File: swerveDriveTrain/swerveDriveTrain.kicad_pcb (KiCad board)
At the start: 4 copper layers, 55 x 125.6 mm, 39 parts, among them IC1 TCAN3414DR, J1 RJ45, J2 Screw_Terminal_01x02, J3 Conn_01x06_Pin, J4 S6B-PH-K-S_LF__SN_, U2 Teensy4.0

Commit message: new outline
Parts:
- J4: moved to B.Cu
- moved J2 215.5 mm to (227.8, 144.4), turned to 0 degrees
- moved U2 211.9 mm to (238.3, 85.1)
- moved J4 186.7 mm to (232.5, 30.7), turned to -90 degrees
- moved U3 185.3 mm to (223.2, 108.4), turned to -90 degrees
- moved J3 178.7 mm to (224.6, 135.0)
- moved U1 135.6 mm to (171.4, 108.3), turned to -90 degrees
- moved J1 135.3 mm to (193.1, 131.6)
- moved IC1 135.3 mm to (197.9, 137.6), turned to 90 degrees
- moved C4 52.2 mm to (113.1, 115.8)
- moved C1 30.2 mm to (115.3, 55.5)
- moved C2 30.2 mm to (115.3, 58.5)
- moved C3 30.2 mm to (115.3, 61.6)
- moved D1 30.2 mm to (139.1, 68.5)
- moved D2 30.2 mm to (139.1, 73.6)
- moved D3 30.2 mm to (139.1, 78.8)
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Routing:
- net +5V: track 109.8 -> 0.00 mm, vias 2 -> 0
- net CAN3v3: track 85.6 -> 0.00 mm, vias 1 -> 0
- net CTX: track 74.7 -> 0.00 mm
- net CRX: track 70.5 -> 0.00 mm
- net M2B: track 43.2 -> 0.00 mm
- net M2A: track 32.8 -> 0.00 mm
- net M1B: track 13.0 -> 0.00 mm
- net M1A: track 9.03 -> 0.00 mm
- net CANN: track 4.70 -> 8.14 mm
- net CANP: track 6.54 -> 7.80 mm
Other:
- board size 55 x 125.6 mm -> 82.5 x 125.6 mm

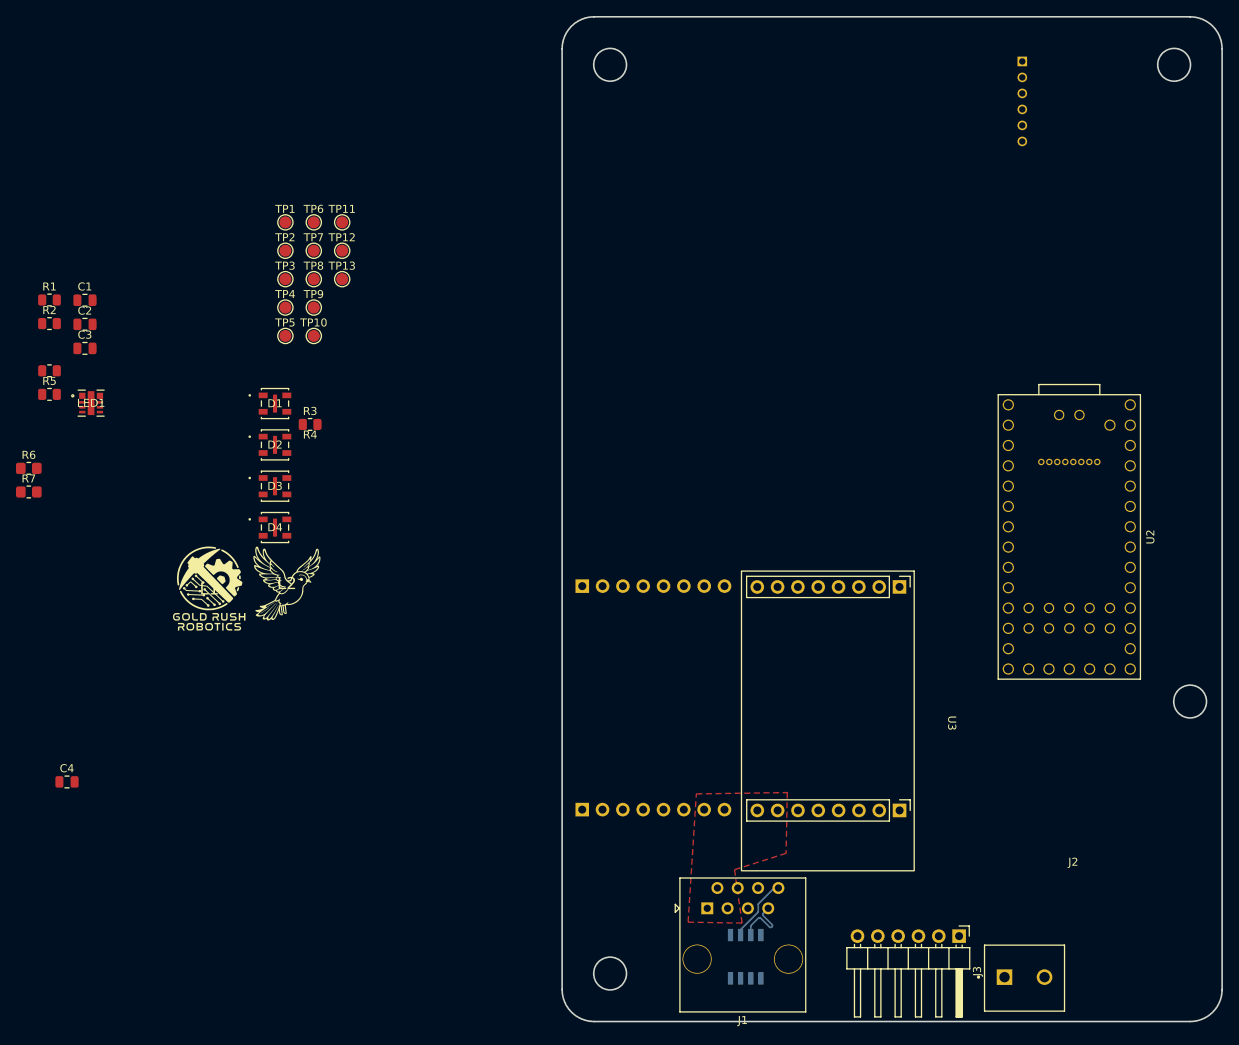
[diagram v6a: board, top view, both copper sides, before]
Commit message: finished first layout and routing pass
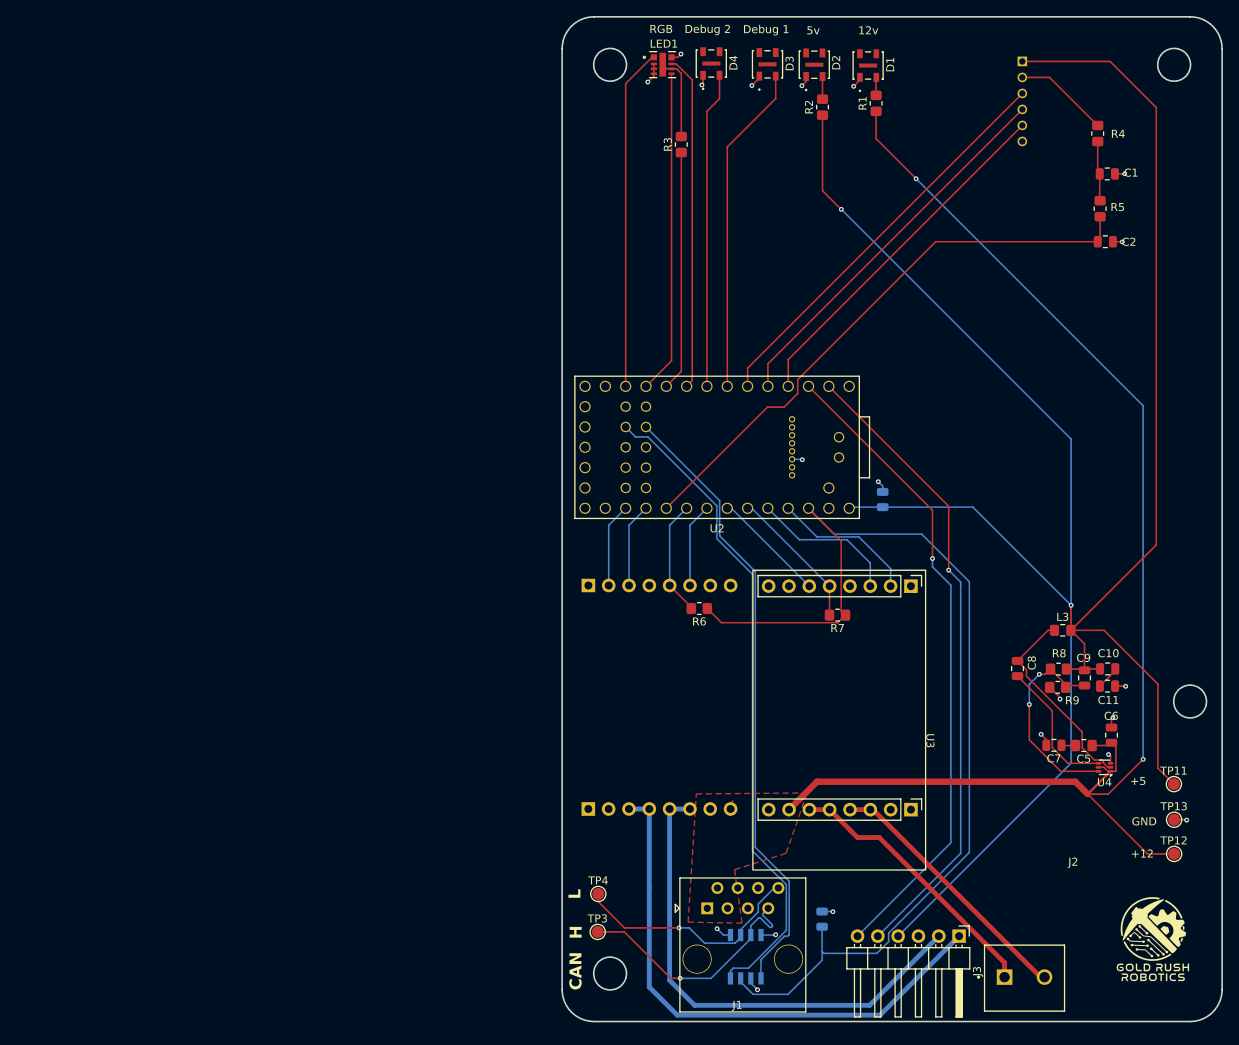
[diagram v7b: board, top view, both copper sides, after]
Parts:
- removed TP1, TP10, TP2, TP5, TP6, TP7, TP8, TP9: TestPoint_Probe, TestPoint:TestPoint_Pad_D1.5mm
- added C10: 22uF, Capacitor_SMD:C_0805_2012Metric, F.Cu at (243.2, 101.6)
- added C11: 22uF, Capacitor_SMD:C_0805_2012Metric, F.Cu at (243.1, 103.8)
- added C5: 10uF, Capacitor_SMD:C_0805_2012Metric_Pad1.18x1.45mm_HandSolder, F.Cu at (240.2, 111.2)
- added C6: 100nF, Capacitor_SMD:C_0805_2012Metric, F.Cu at (243.6, 109.9)
- added C7: 10uF, Capacitor_SMD:C_0805_2012Metric, F.Cu at (236.4, 111.2)
- added C8: 100nF, Capacitor_SMD:C_0805_2012Metric, F.Cu at (231.9, 101.6)
- added C9: 22pF, Capacitor_SMD:C_0805_2012Metric, F.Cu at (240.2, 102.8)
- added L3: 4.7uH, Inductor_SMD:L_0805_2012Metric_Pad1.15x1.40mm_HandSolder, F.Cu at (237.5, 96.8)
- added R8: 52.3kΩ, Resistor_SMD:R_0805_2012Metric_Pad1.20x1.40mm_HandSolder, F.Cu at (237.0, 101.7)
- added R9: 10kΩ, Resistor_SMD:R_0805_2012Metric_Pad1.20x1.40mm_HandSolder, F.Cu at (236.9, 103.9)
- added U4: TPS562202, Package_TO_SOT_SMD:SOT-563, F.Cu at (242.8, 113.9)
- C3, C4, L2: moved to B.Cu
- R1, R2, R3, R4, R5: footprint Resistor_SMD:R_0805_2012Metric -> Resistor_SMD:R_0805_2012Metric_Pad1.20x1.40mm_HandSolder
- moved R4 134.3 mm to (241.9, 34.7), turned to -90 degrees
- moved R5 133.4 mm to (242.2, 44.1), turned to -90 degrees
- moved C1 128.8 mm to (243.1, 39.8), turned to 180 degrees
- moved TP12 128.4 mm to (251.4, 124.8)
- moved C2 128.0 mm to (242.8, 48.2)
- moved L1 125.8 mm to (248.8, 135.4)
- moved TP11 125.5 mm to (251.4, 116.0)
- moved TP13 124.0 mm to (251.4, 120.5)
- moved R1 106.2 mm to (214.2, 30.9), turned to 90 degrees
- moved R7 102.3 mm to (209.4, 94.9), turned to 180 degrees
- moved C3 101.5 mm to (215.0, 80.5), turned to 90 degrees
- moved R2 100.3 mm to (207.5, 31.4), turned to 90 degrees
- moved C4 95.9 mm to (207.4, 132.9), turned to -90 degrees
- moved TP3 90.5 mm to (179.4, 134.5)
- moved L2 88.9 mm to (228.2, 76.2), turned to 180 degrees
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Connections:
- R6 pad 1: +3.3V -> CAN3v3
- R7 pad 1: +3.3V -> CAN3v3
- U2 pad 10: ENC1A -> RGBR
- U2 pad 11: ENC1B -> RGBG
- U2 pad 12: ENC2I -> RGBW
- U2 pad 13: ENC2A -> unconnected-(U2-11_MOSI_CTX1-Pad13)
- U2 pad 14: ENC2B -> unconnected-(U2-12_MISO_MQSL-Pad14)
- U2 pad 2: PWM1 -> ENC1A
- U2 pad 21: ABSA -> unconnected-(U2-14_A0_TX3_SPDIF_OUT-Pad21)
- U2 pad 22: CSM1 -> DIR1
- U2 pad 23: CSM2 -> PWM1
- U2 pad 24: unconnected-(U2-17_A3_TX4_SDA1-Pad24) -> ABSA
- U2 pad 25: DIR1 -> FLTM1
- U2 pad 26: DIR2 -> CSM1
- U2 pad 27: FLTM1 -> CSM2
- U2 pad 29: unconnected-(U2-22_A8_CTX1-Pad29) -> PWM2
- U2 pad 3: PWM2 -> ENC1B
- U2 pad 30: unconnected-(U2-23_A9_CRX1_MCLK1-Pad30) -> DIR2
- U2 pad 4: RGBR -> ENC2I
- U2 pad 5: RGBG -> ENC2B
- U2 pad 6: RGBB -> ENC2A
- U2 pad 7: RGBW -> LED1
- U2 pad 8: LED1 -> LED2
- U2 pad 9: LED2 -> RGBB
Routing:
- net +5V: track 0.00 -> 286.4 mm, vias 0 -> 2
- net +12V: track 0.00 -> 171.1 mm, vias 0 -> 2
- net CAN3v3: track 0.00 -> 133.0 mm
- net CRX: track 0.00 -> 82.2 mm
- net ENC1B: track 0.00 -> 80.9 mm, vias 0 -> 1
- net ENC1A: track 0.00 -> 79.8 mm, vias 0 -> 1
- net CTX: track 0.00 -> 78.0 mm
- net ABSA: track 0.00 -> 72.0 mm
- net M1A: track 0.00 -> 69.1 mm
- net M1B: track 0.00 -> 62.5 mm
- net ENC2A: track 0.00 -> 50.8 mm
- net ENC2B: track 0.00 -> 47.8 mm
- net ENC2I: track 0.00 -> 44.7 mm
- net RGBW: track 0.00 -> 42.7 mm
- net RGBB: track 0.00 -> 42.0 mm
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- added copper zone on In1.Cu, net GND
- added copper zone on In2.Cu, net GND
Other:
- board text added: "+12"
- board text added: "+5"
- board text added: "12v"
- board text added: "5v"
- board text added: "CAN"
- board text added: "Debug 1"
- board text added: "Debug 2"
- board text added: "GND"
- board text added: "H"
- board text added: "L"
- board text added: "RGB"

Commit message: cleaning
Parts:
- removed C10, C11: 22uF, Capacitor_SMD:C_0805_2012Metric
- removed C5: 10uF, Capacitor_SMD:C_0805_2012Metric_Pad1.18x1.45mm_HandSolder
- removed C6, C8: 100nF, Capacitor_SMD:C_0805_2012Metric
- removed C7: 10uF, Capacitor_SMD:C_0805_2012Metric
- removed C9: 22pF, Capacitor_SMD:C_0805_2012Metric
- removed L3: 4.7uH, Inductor_SMD:L_0805_2012Metric_Pad1.15x1.40mm_HandSolder
- removed LED1: 599-2310-427F, footprints:599-2310_DIA
- removed R9: 10kΩ, Resistor_SMD:R_0805_2012Metric_Pad1.20x1.40mm_HandSolder
- removed TP3, TP4: TestPoint_Probe, TestPoint:TestPoint_Pad_D1.5mm
- removed U4: TPS562202, Package_TO_SOT_SMD:SOT-563
- C1, C2, C3, C4: footprint Capacitor_SMD:C_0805_2012Metric -> Capacitor_SMD:C_0805_2012Metric_Pad1.18x1.45mm_HandSolder
- D1, D2, D3, D4: footprint GreenLED:LED_CREE_MLXXXX -> LED_SMD:LED_0805_2012Metric_Pad1.15x1.40mm_HandSolder
- R1: value 25 -> 500
- R2: value 5 -> 150
- R3: value 15 -> 50
- R6, R7: value R -> 10k
- R8: value 52.3kΩ -> 50
- U1, U3: value ~ -> G218v17
- moved R8 81.0 mm to (195.2, 32.3), turned to -90 degrees
- moved C4 13.3 mm to (198.1, 142.3), turned to 180 degrees
- moved R3 9.17 mm to (198.2, 32.3), turned to -90 degrees
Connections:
- D3 pad 2: LED1 -> Net-(D3-A)
- D4 pad 2: LED2 -> Net-(D4-A)
- R3 pad 1: RGBR -> Net-(D3-A)
- R3 pad 2: Net-(LED1-Pad5) -> LED1
- R8 pad 1: +5V -> Net-(D4-A)
- R8 pad 2: Net-(U4-VFB) -> LED2
- U2 pad 10: RGBR -> unconnected-(U2-8_TX2_IN1-Pad10)
- U2 pad 11: RGBG -> unconnected-(U2-9_OUT1C-Pad11)
- U2 pad 12: RGBW -> unconnected-(U2-10_CS_MQSR-Pad12)
- U2 pad 9: RGBB -> unconnected-(U2-7_RX2_OUT1A-Pad9)
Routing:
- net +12V: track 171.1 -> 1.49 mm, vias 2 -> 0
- net +5V: track 286.4 -> 131.8 mm, vias 2 -> 1
- net RGBW: track 42.7 -> 0.00 mm
- net RGBB: track 42.0 -> 0.00 mm
- net LED1: track 41.3 -> 0.00 mm
- net RGBG: track 40.4 -> 0.00 mm
- net LED2: track 39.5 -> 0.00 mm
- net RGBR: track 30.0 -> 0.00 mm
- net Net-(U4-VFB): track 26.2 -> 0.00 mm, vias 2 -> 0
- net Net-(U4-SW): track 25.1 -> 0.00 mm
- net CANP: track 32.0 -> 7.80 mm, vias 1 -> 0
- net CANN: track 29.7 -> 8.14 mm, vias 1 -> 0
- net Net-(U4-VBST): track 17.4 -> 0.00 mm
- net GND: track 30.9 -> 14.4 mm, vias 20 -> 8
- net Net-(LED1-Pad5): track 10.7 -> 0.00 mm
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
